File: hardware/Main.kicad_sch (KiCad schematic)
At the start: 23 parts, among them IC102 APDS-9306-065, IC103 BME688, M101 BL54L15, Q101 BSS84, SW101 JOIN, X102 DEBUG

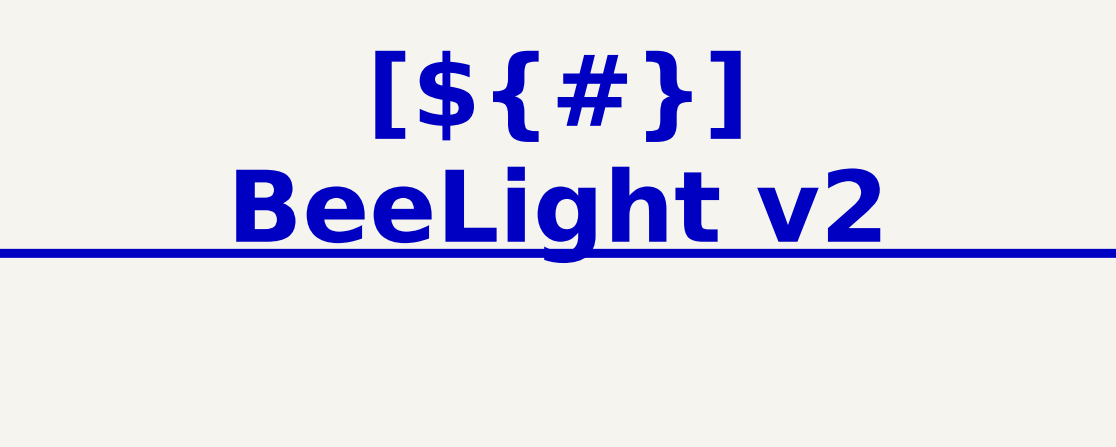
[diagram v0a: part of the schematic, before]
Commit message: Implement new CI/CD workflow
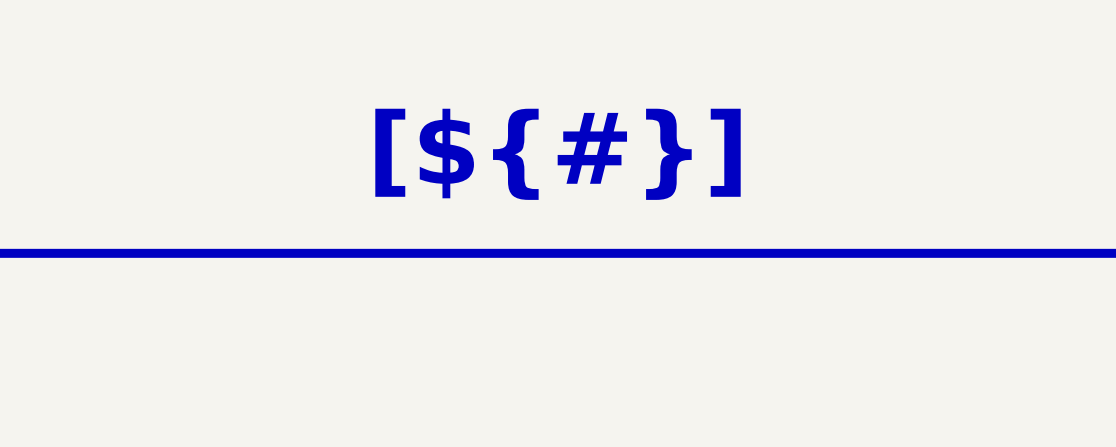
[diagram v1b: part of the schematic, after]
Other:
- title: BeeLight v2 -> (none)
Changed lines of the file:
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@@
 	(paper "A3")
 	(title_block
-		(title "BeeLight v2")
 		(date "2025-06-05")
 		(rev "${REVISION}")
